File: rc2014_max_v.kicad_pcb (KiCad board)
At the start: 2 copper layers, 101.6 x 50.8 mm, 119 parts, among them J1 M3 Mounting Hole, J2 Conn_01x40, J3 Pro Bus, J4 Conn_01x24, J5 AVR-JTAG-10, J6 USB_B_Micro, J7 PMOD1, J8 PMOD, SW1 SW_Push, SW2 SW_Push, U1 TXB0108PWR, U10 93LCxxBxxOT, U11 MIC5356-SGYMME, U12 IS61LV5128AL-10TLI, U13 Si5351A-B-GT, U2 SN74ALVC164245DGG, U3 SN74ALVC164245DGG, U4 5M1270ZT144C5N, U5 TXB0108PWR, U6 SN74ALVC164245DGG, U7 MIC5356-SGYMME, U8 TPD2EUSB30, U9 FT2232H, X1 CB3LV-3I-50M0000, Y2 25MHZ 8PF

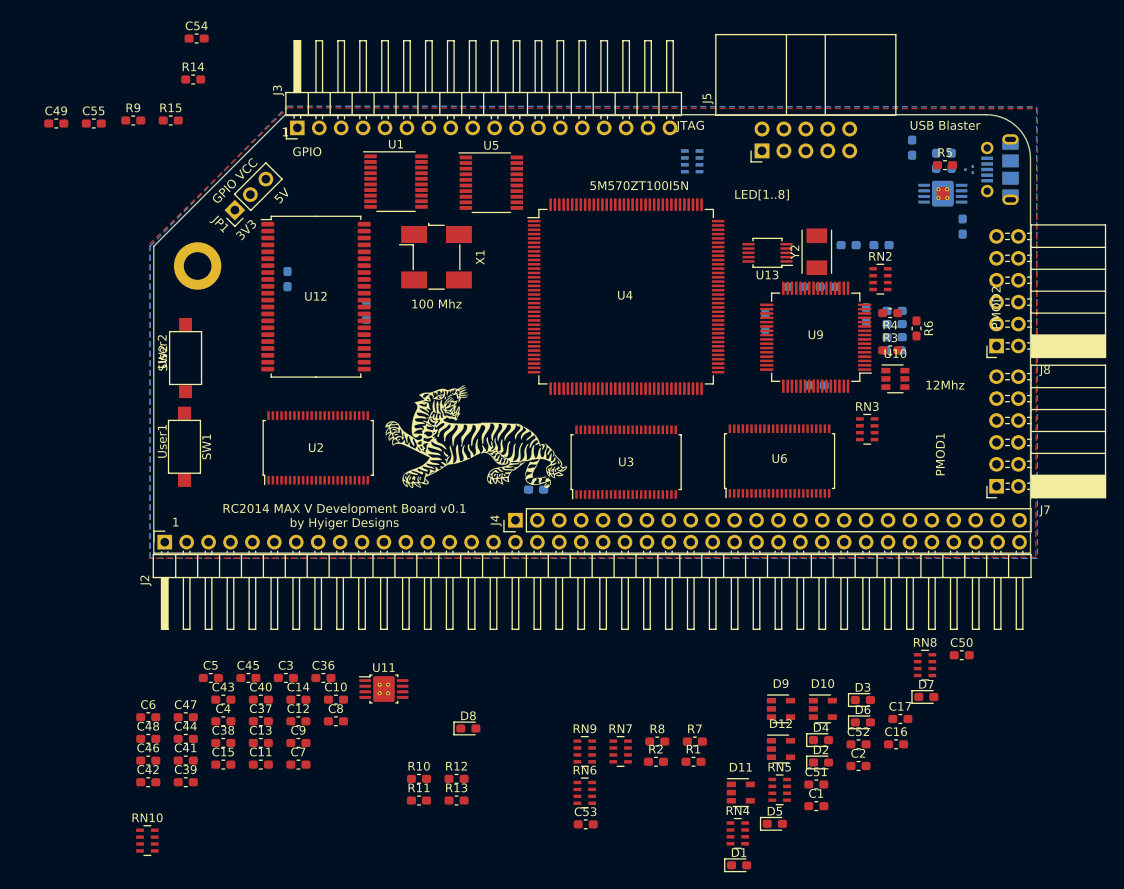
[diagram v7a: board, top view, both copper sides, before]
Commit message: component placement
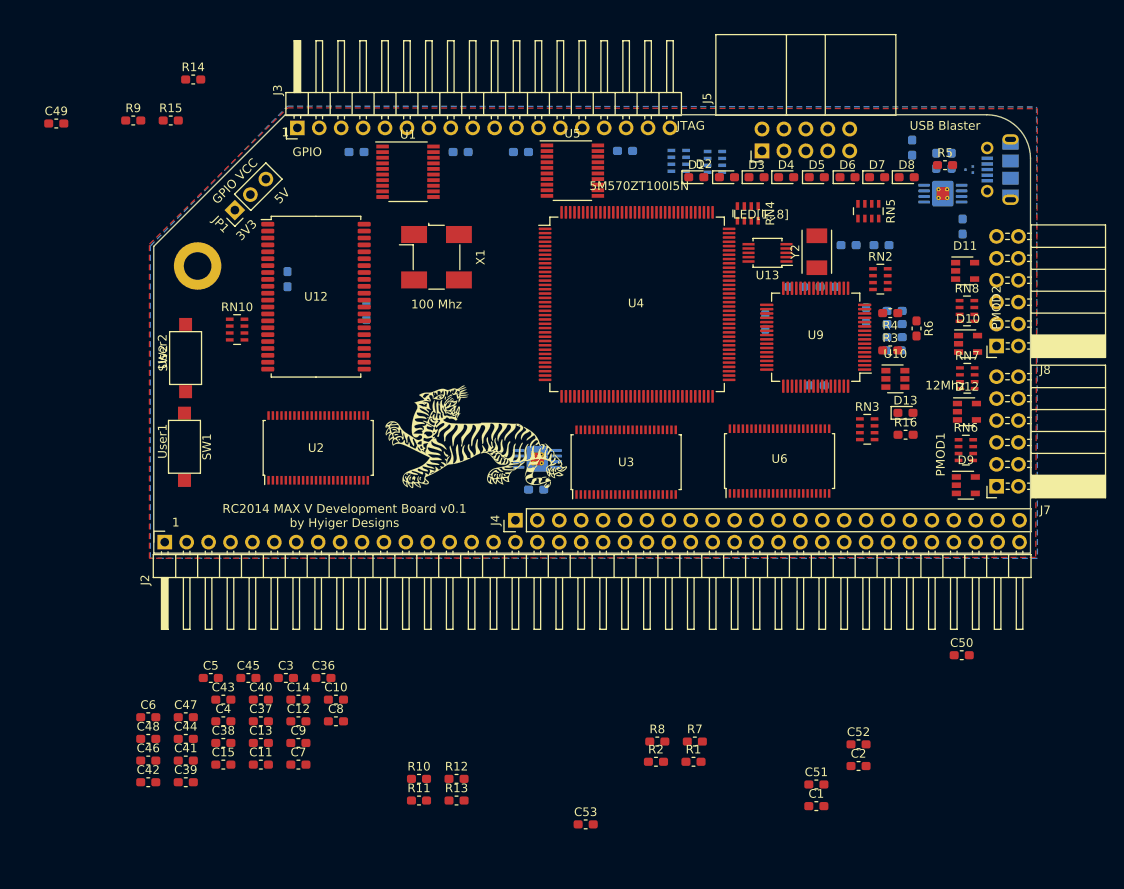
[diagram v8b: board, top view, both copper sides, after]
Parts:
- added D13: PWR, LED_SMD:LED_0603_1608Metric_Pad1.05x0.95mm_HandSolder, F.Cu at (162.5, 111.3)
- added R16: 220R, Resistor_SMD:R_0603_1608Metric_Pad1.05x0.95mm_HandSolder, F.Cu at (162.6, 113.8)
- C16, C17, C54, C55, RN9, U11: moved to B.Cu
- moved C16 85.2 mm to (111.0, 81.0)
- moved D8 81.6 mm to (162.7, 83.9)
- moved D1 79.9 mm to (138.3, 83.9)
- moved D5 75.1 mm to (152.3, 83.9)
- moved C17 73.2 mm to (130.0, 80.9)
- moved RN4 71.9 mm to (144.3, 88.1), turned to 270 degrees
- moved RN9 70.0 mm to (140.5, 82.2), turned to 180 degrees
- moved D2 68.7 mm to (141.9, 83.9)
- moved RN5 67.8 mm to (158.2, 87.9), turned to 270 degrees
- moved D11 65.8 mm to (169.5, 94.8)
- moved D4 65.4 mm to (148.7, 83.9)
- moved D6 63.2 mm to (155.8, 83.9)
- moved D3 61.8 mm to (145.3, 83.9)
- moved D7 60.5 mm to (159.3, 83.9)
- moved RN10 60.1 mm to (85.1, 101.6)
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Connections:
- J2 pad 35: (no net) -> TX_A
- J2 pad 37: (no net) -> Net-(J2-Pad37)
- J2 pad 38: (no net) -> Net-(J2-Pad38)
- J2 pad 39: (no net) -> Net-(J2-Pad39)
- J2 pad 40: (no net) -> Net-(J2-Pad40)
- J4 pad 19: (no net) -> TX_B
- J4 pad 20: (no net) -> RX_B
- J4 pad 21: (no net) -> Net-(J4-Pad21)
- J4 pad 22: (no net) -> Net-(J4-Pad22)
- J4 pad 23: (no net) -> Net-(J4-Pad23)
- J4 pad 24: (no net) -> Net-(J4-Pad24)
- J4 pad 3: (no net) -> ~RFSH
- J4 pad 5: (no net) -> CLK2
- J5 pad 7: (no net) -> Net-(J5-Pad7)
- J5 pad 8: (no net) -> Net-(J5-Pad8)
- RN10 pad 4: (no net) -> Net-(RN10-Pad4)
- RN3 pad 4: (no net) -> Net-(RN3-Pad4)
- RN4 pad 1: Net-(D1-Pad2) -> Net-(D4-Pad2)
- RN4 pad 2: Net-(D2-Pad2) -> Net-(D3-Pad2)
- RN4 pad 3: Net-(D3-Pad2) -> Net-(D2-Pad2)
- RN4 pad 4: Net-(D4-Pad2) -> Net-(D1-Pad2)
- RN5 pad 1: Net-(D5-Pad2) -> Net-(D8-Pad2)
- RN5 pad 2: Net-(D6-Pad2) -> Net-(D7-Pad2)
- RN5 pad 3: Net-(D7-Pad2) -> Net-(D6-Pad2)
- RN5 pad 4: Net-(D8-Pad2) -> Net-(D5-Pad2)
- U11 pad 6: (no net) -> Net-(U11-Pad6)
- U12 pad 1: (no net) -> Net-(U12-Pad1)
- U12 pad 2: (no net) -> Net-(U12-Pad2)
- U12 pad 21: (no net) -> Net-(U12-Pad21)
- U12 pad 22: (no net) -> Net-(U12-Pad22)
- U12 pad 23: (no net) -> Net-(U12-Pad23)
- U12 pad 24: (no net) -> Net-(U12-Pad24)
- U12 pad 25: (no net) -> Net-(U12-Pad25)
- U12 pad 39: (no net) -> Net-(U12-Pad39)
- U12 pad 40: (no net) -> Net-(U12-Pad40)
- U12 pad 41: (no net) -> Net-(U12-Pad41)
- U12 pad 42: (no net) -> Net-(U12-Pad42)
- U12 pad 43: (no net) -> Net-(U12-Pad43)
- U12 pad 44: (no net) -> Net-(U12-Pad44)
- U3 pad 1: (no net) -> DIR_C_O
- U3 pad 24: (no net) -> DIR_C_I
- U3 pad 37: (no net) -> RX_A_F
- U3 pad 5: (no net) -> ~RESET2
- U4 pad 4: (no net) -> Net-(U4-Pad4)
- U4 pad 5: (no net) -> Net-(U4-Pad5)
- U4 pad 51: (no net) -> Net-(U4-Pad51)
- U4 pad 52: (no net) -> Net-(U4-Pad52)
- U4 pad 73: (no net) -> Net-(U4-Pad73)
- U4 pad 74: (no net) -> Net-(U4-Pad74)
- U4 pad 75: (no net) -> Net-(U4-Pad75)
- U4 pad 76: (no net) -> Net-(U4-Pad76)
- U4 pad 77: (no net) -> Net-(U4-Pad77)
- U4 pad 79: (no net) -> Net-(U4-Pad79)
- U4 pad 80: (no net) -> Net-(U4-Pad80)
- U4 pad 81: (no net) -> Net-(U4-Pad81)
- U4 pad 84: (no net) -> Net-(U4-Pad84)
- U4 pad 85: (no net) -> Net-(U4-Pad85)
- U4 pad 86: (no net) -> Net-(U4-Pad86)
- U4 pad 87: (no net) -> Net-(U4-Pad87)
- U4 pad 88: (no net) -> Net-(U4-Pad88)
- U4 pad 93: (no net) -> Net-(U4-Pad93)
- U4 pad 94: (no net) -> Net-(U4-Pad94)
- U4 pad 95: (no net) -> Net-(U4-Pad95)
- U4 pad 96: (no net) -> Net-(U4-Pad96)
- U7 pad 6: (no net) -> Net-(U7-Pad6)
- U9 pad 21: (no net) -> Net-(U9-Pad21)
- U9 pad 22: (no net) -> Net-(U9-Pad22)
- U9 pad 23: (no net) -> Net-(U9-Pad23)
- U9 pad 24: (no net) -> Net-(U9-Pad24)
- U9 pad 26: (no net) -> Net-(U9-Pad26)
- U9 pad 27: (no net) -> Net-(U9-Pad27)
- U9 pad 28: (no net) -> Net-(U9-Pad28)
- U9 pad 29: (no net) -> Net-(U9-Pad29)
- U9 pad 3: (no net) -> Net-(U9-Pad3)
- U9 pad 30: (no net) -> Net-(U9-Pad30)
- U9 pad 32: (no net) -> Net-(U9-Pad32)
- U9 pad 33: (no net) -> Net-(U9-Pad33)
- U9 pad 34: (no net) -> Net-(U9-Pad34)
- U9 pad 36: (no net) -> Net-(U9-Pad36)
- U9 pad 38: (no net) -> Net-(U9-Pad38)
- U9 pad 39: (no net) -> Net-(U9-Pad39)
- U9 pad 40: (no net) -> Net-(U9-Pad40)
- U9 pad 41: (no net) -> Net-(U9-Pad41)
- U9 pad 43: (no net) -> Net-(U9-Pad43)
- U9 pad 44: (no net) -> Net-(U9-Pad44)
- U9 pad 45: (no net) -> Net-(U9-Pad45)
- U9 pad 46: (no net) -> Net-(U9-Pad46)
- U9 pad 48: (no net) -> Net-(U9-Pad48)
- U9 pad 49: (no net) -> Net-(U9-Pad49)
- U9 pad 50: (no net) -> Net-(U9-Pad50)
- U9 pad 52: (no net) -> Net-(U9-Pad52)
- U9 pad 53: (no net) -> Net-(U9-Pad53)
- U9 pad 54: (no net) -> Net-(U9-Pad54)
- U9 pad 55: (no net) -> Net-(U9-Pad55)
- U9 pad 57: (no net) -> Net-(U9-Pad57)
- U9 pad 58: (no net) -> Net-(U9-Pad58)
- U9 pad 59: (no net) -> Net-(U9-Pad59)
- U9 pad 60: (no net) -> Net-(D13-Pad1)
